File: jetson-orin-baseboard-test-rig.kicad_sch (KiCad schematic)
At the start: 83 parts, among them J1 PinHeader_2x6_P2.54mm_Drill1.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, J10 Harwin_1x1_H17.75mm_Drill0.8m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, J11 Harwin_1x1_H17.75mm_Drill0.8m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, J12 Harwin_1x1_H17.75mm_Drill0.8m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, J13 Harwin_1x1_H17.75mm_Drill0.8m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, J14 Harwin_1x1_H17.75mm_Drill0.8m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, J15 Harwin_1x1_H17.75mm_Drill0.8m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, J16 Harwin_1x1_H17.75mm_Drill0.8m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, J17 Harwin_1x1_H17.75mm_Drill0.8m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, J18 Harwin_1x1_H17.75mm_Drill0.8m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, J19 Harwin_1x1_H17.75mm_Drill0.8m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, J2 PinHeader_2x6_P2.54mm_Drill1.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, J20 Harwin_1x1_H17.75mm_Drill0.8m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, J21 Harwin_1x1_H17.75mm_Drill0.8m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, J22 Harwin_1x1_H17.75mm_Drill0.8m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, J23 Harwin_1x1_H17.75mm_Drill0.8m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, J24 Harwin_1x1_H17.75mm_Drill0.8m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, J25 Harwin_1x1_H17.75mm_Drill0.8m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, J26 Harwin_1x1_H17.75mm_Drill0.8m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, J27 Harwin_1x1_H17.75mm_Drill0.8m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, J28 Harwin_1x1_H17.75mm_Drill0.8m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, J29 Harwin_1x1_H17.75mm_Drill0.8m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, J3 PinHeader_2x6_P2.54mm_Drill1.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, J30 Harwin_1x1_H17.75mm_Drill0.8m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, J4 PinHeader_2x6_P2.54mm_Drill1.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, J5 PinHeader_2x6_P2.54mm_Drill1.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, J6 PinHeader_2x6_P2.54mm_Drill1.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, J7 PinHeader_2x6_P2.54mm_Drill1.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, J8 Harwin_1x1_H17.75mm_Drill0.8m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, J9 Harwin_1x1_H17.75mm_Drill0.8m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, Q1 BSS84

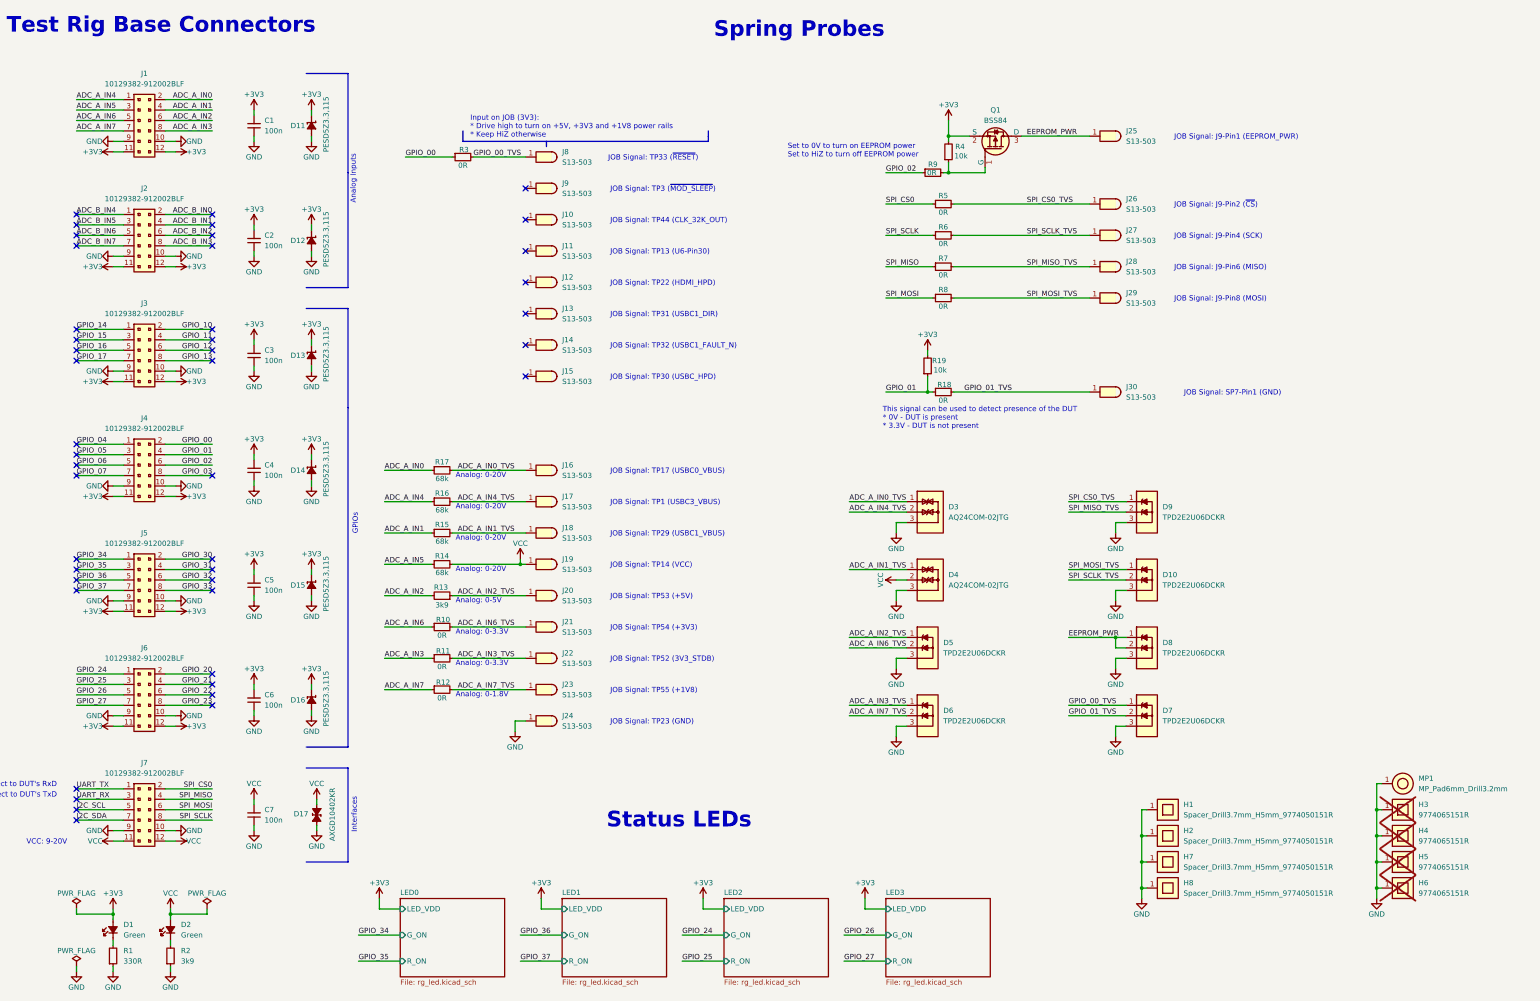
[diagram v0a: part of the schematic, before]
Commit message: [#79468] Add I2C pins to SCH
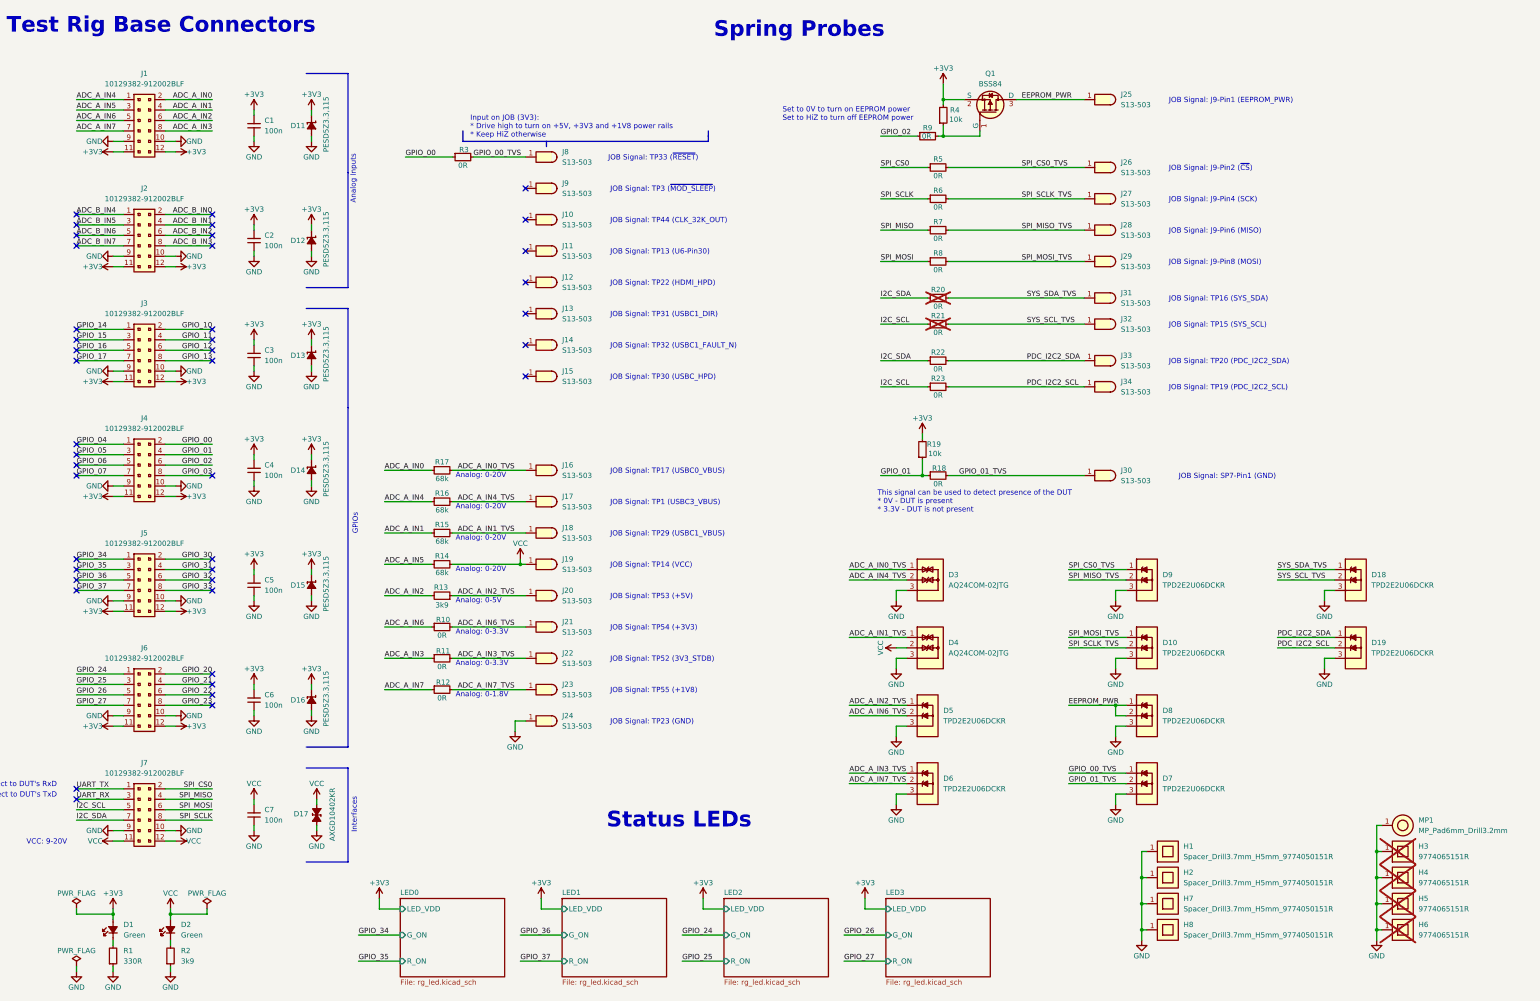
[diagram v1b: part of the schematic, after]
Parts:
- added D18, D19: TPD2E2U06_SC70, antmicro-footprints:SC70-3, symbol antmicroTVSDiodes:TPD2E2U06_SC70
- added J31, J32: Harwin_1x1_H17.75mm_Drill0.8mm_S13-503_CUSTOM, antmicro-footprints:PogoPin_Harwin_1x1_H17.75mm_Drill0.8mm_S13-503, symbol antmicroPogoPins:Harwin_1x1_H17.75mm_Drill0.8mm_S13-503_CUSTOM
- added J33, J34: Harwin_1x1_H17.75mm_Drill0.8mm_S13-503_CUSTOM_Obl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, antmicro-footprints:PogoPin_Harwin_1x1_H17.75mm_Drill0.8mm_CUSTOM_S13-503, symbol antmicroPogoPins:Harwin_1x1_H17.75mm_Drill0.8mm_S13-503_CUSTOM_Oblong
- added R20, R21, R22, R23: R_0R_0402, antmicro-footprints:R_0402_1005Metric, symbol antmicroResistors0402:R_0R_0402
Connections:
- net GND: now also D18.3, D19.3
- net I2C_SCL: now also R21.1, R23.1
- net I2C_SDA: now also R20.1, R22.1
- new net PDC_I2C2_SCL: D19.2, J34.1, R23.2
- new net PDC_I2C2_SDA: D19.1, J33.1, R22.2
- new net SYS_SCL_TVS: D18.2, J32.1, R21.2
- new net SYS_SDA_TVS: D18.1, J31.1, R20.2
- no-connect marks 44 -> 42
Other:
- note added: "JOB Signal: TP15 (SYS_SCL)"
- note added: "JOB Signal: TP16 (SYS_SDA)"
- note added: "JOB Signal: TP19 (PDC_I2C2_SCL)"
- note added: "JOB Signal: TP20 (PDC_I2C2_SDA)"
- moved on the sheet: D10, D3, D4, D5, D6, D7, D8, D9, H1, H2, H3, H4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

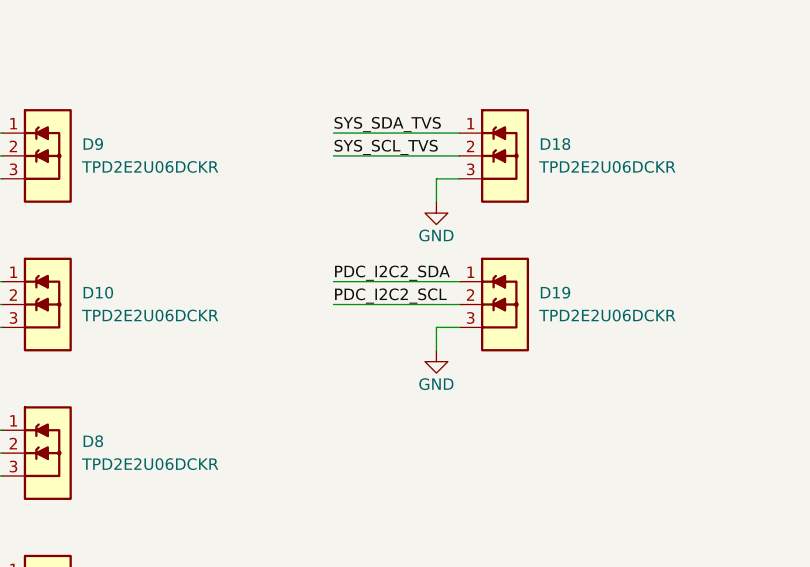
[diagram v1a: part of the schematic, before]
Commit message: [#79468] Position pins on the PCB
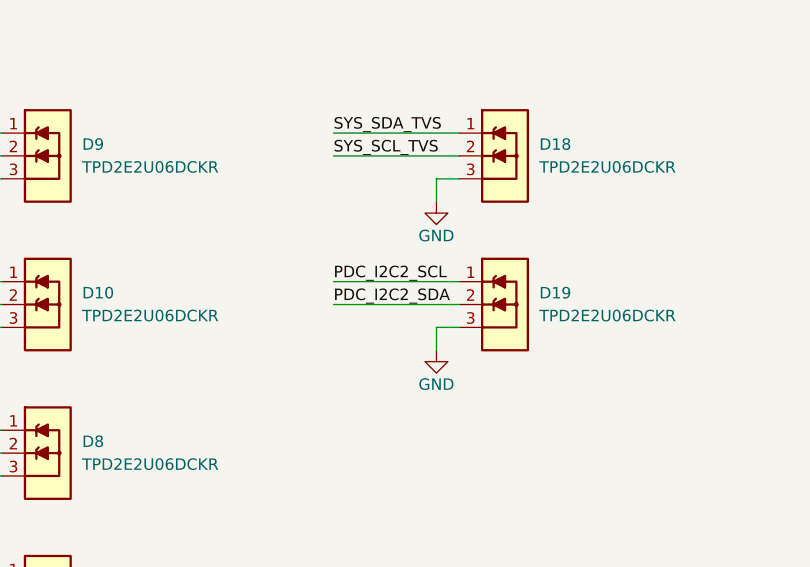
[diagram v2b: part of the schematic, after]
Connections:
- net PDC_I2C2_SCL: now also D19.1; no longer D19.2
- net PDC_I2C2_SDA: now also D19.2; no longer D19.1
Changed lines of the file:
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@@
 	)
 	(label "PDC_I2C2_SCL"
-		(at 342.9 176.53 0)
+		(at 342.9 173.99 0)
 		(effects
 			(font
@@
 	)
 	(label "PDC_I2C2_SDA"
-		(at 342.9 173.99 0)
+		(at 342.9 176.53 0)
 		(effects
 			(font
